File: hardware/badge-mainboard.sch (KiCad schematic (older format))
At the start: 11 parts

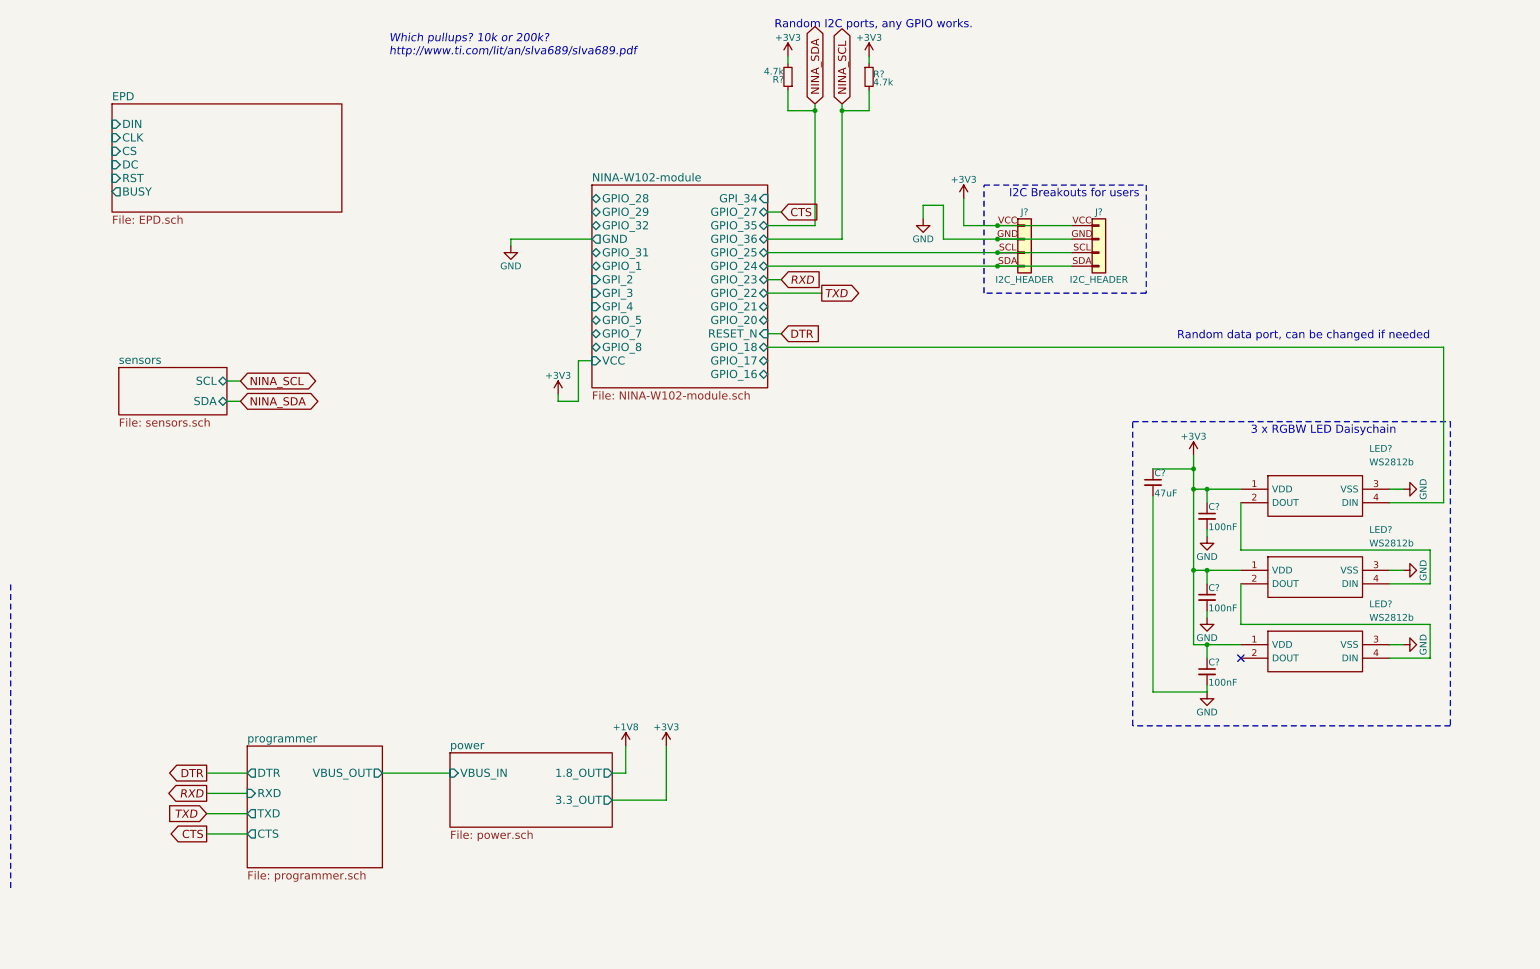
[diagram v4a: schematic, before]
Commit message: Added 4 user buttons
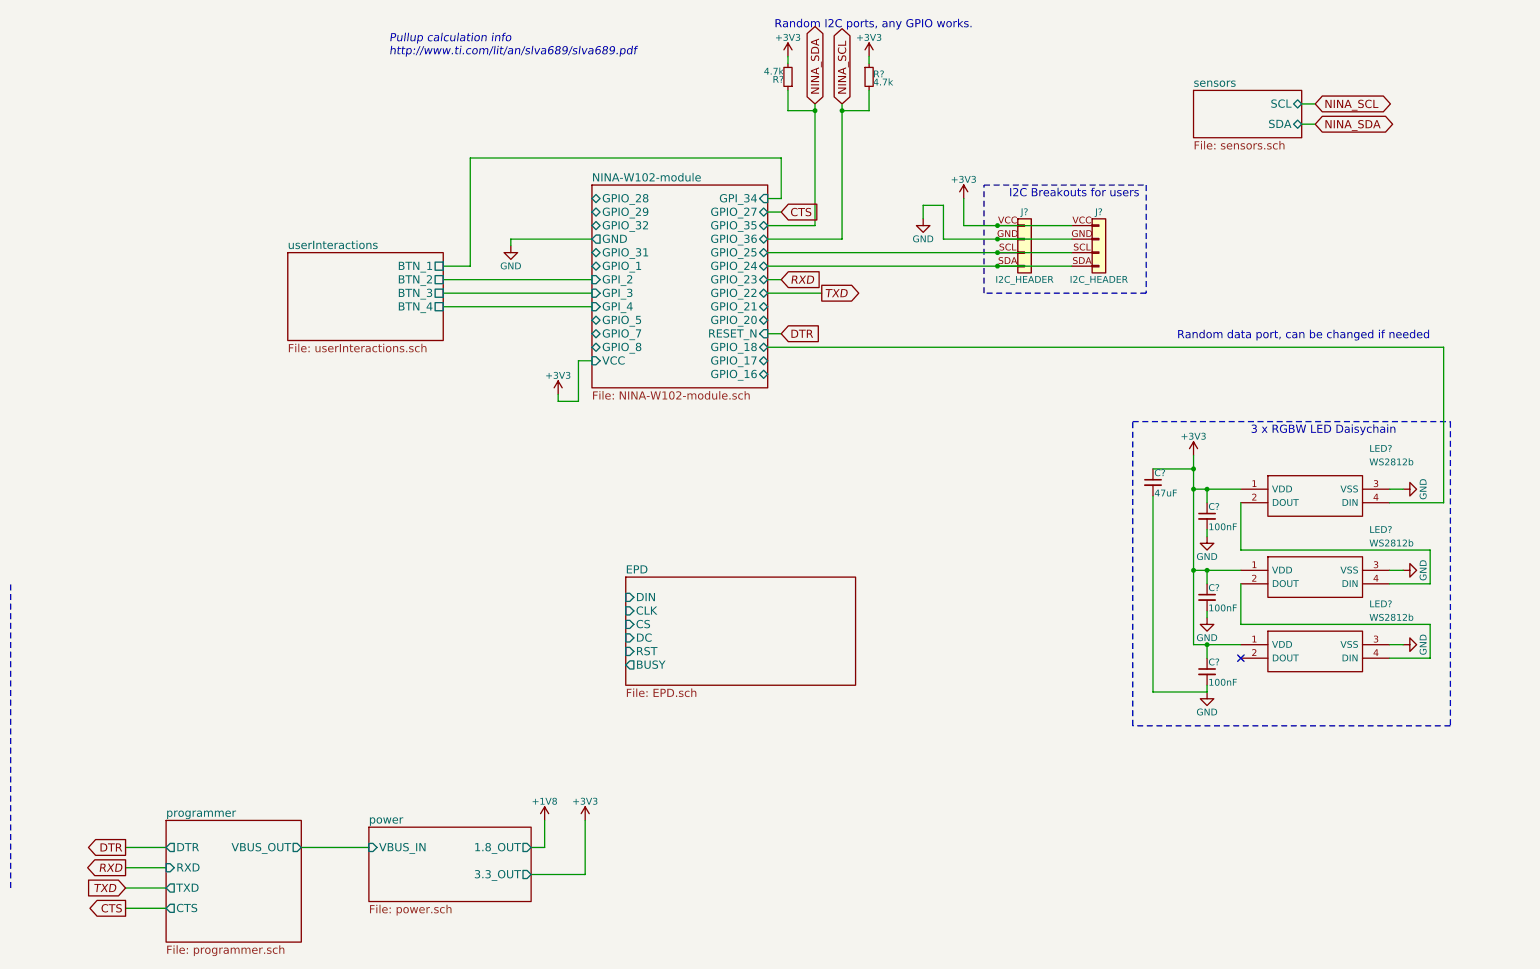
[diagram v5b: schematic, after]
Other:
- note added: "Pullup calculation info\nhttp://www.ti.com/lit/an/slva689/slva689.pdf"
- note removed: "Which pullups? 10k or 200k?\nhttp://www.ti.com/lit/an/slva689/slva689.pdf"
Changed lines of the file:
@@
 $Descr A4 11693 8268
 encoding utf-8
-Sheet 1 6
+Sheet 1 7
 Title "IoT conference badge - mainboard"
 Date "2018-04-09"
@@
 $EndComp
 Text Notes 3300 800  0    60   Italic 0
-Which pullups? 10k or 200k?\nhttp://www.ti.com/lit/an/slva689/slva689.pdf
+Pullup calculation info\nhttp://www.ti.com/lit/an/slva689/slva689.pdf
 $Sheet
-S 1300 3100 800  350
+S 9250 1050 800  350
 U 5AD378C9
 F0 "sensors" 60
 F1 "sensors.sch" 60
-F2 "SCL" B R 2100 3200 60
-F3 "SDA" B R 2100 3350 60
+F2 "SCL" B R 10050 1150 60
+F3 "SDA" B R 10050 1300 60
 $EndSheet
-Text GLabel 2200 3350 2    60   BiDi ~ 0
+Text GLabel 10150 1300 2    60   BiDi ~ 0
 NINA_SDA
-Text GLabel 2200 3200 2    60   BiDi ~ 0
+Text GLabel 10150 1150 2    60   BiDi ~ 0
 NINA_SCL
 $Sheet
-S 2250 5900 1000 900
+S 1650 6450 1000 900
 U 5AD3BA03
 F0 "programmer" 60
 F1 "programmer.sch" 60
-F2 "DTR" O L 2250 6100 60
-F3 "RXD" I L 2250 6250 60
-F4 "TXD" O L 2250 6400 60
-F5 "CTS" O L 2250 6550 60
-F6 "VBUS_OUT" O R 3250 6100 60
+F2 "DTR" O L 1650 6650 60
+F3 "RXD" I L 1650 6800 60
+F4 "TXD" O L 1650 6950 60
+F5 "CTS" O L 1650 7100 60
+F6 "VBUS_OUT" O R 2650 6650 60
 $EndSheet
-Text GLabel 1950 6400 0    60   Input Italic 0
+Text GLabel 1350 6950 0    60   Input Italic 0
 TXD
-Text GLabel 1950 6250 0    60   Output Italic 0
+Text GLabel 1350 6800 0    60   Output Italic 0
 RXD
 $Sheet
-S 1250 1150 1700 800
+S 5050 4650 1700 800
 U 5AD3E430
 F0 "EPD" 60
 F1 "EPD.sch" 60
-F2 "DIN" I L 1250 1300 60
-F3 "CLK" I L 1250 1400 60
-F4 "CS" I L 1250 1500 60
-F5 "DC" I L 1250 1600 60
-F6 "RST" I L 1250 1700 60
-F7 "BUSY" O L 1250 1800 60
+F2 "DIN" I L 5050 4800 60
+F3 "CLK" I L 5050 4900 60
+F4 "CS" I L 5050 5000 60
+F5 "DC" I L 5050 5100 60
+F6 "RST" I L 5050 5200 60
+F7 "BUSY" O L 5050 5300 60
 $EndSheet
 $Sheet
-S 3750 5950 1200 550
+S 3150 6500 1200 550
 U 5AD42326
 F0 "power" 60
 F1 "power.sch" 60
-F2 "VBUS_IN" I L 3750 6100 60
-F3 "1.8_OUT" O R 4950 6100 60
-F4 "3.3_OUT" O R 4950 6300 60
+F2 "VBUS_IN" I L 3150 6650 60
+F3 "1.8_OUT" O R 4350 6650 60
+F4 "3.3_OUT" O R 4350 6850 60
 $EndSheet
 $Comp
 L +1V8 #PWR08
 U 1 1 5AD43521
-P 5050 5900
-F 0 "#PWR08" H 5050 5750 50  0001 C CNN
-F 1 "+1V8" H 5050 6040 50  0000 C CNN
-F 2 "" H 5050 5900 50  0001 C CNN
-F 3 "" H 5050 5900 50  0001 C CNN
-	1    5050 5900
+P 4450 6450
+F 0 "#PWR08" H 4450 6300 50  0001 C CNN
+F 1 "+1V8" H 4450 6590 50  0000 C CNN
+F 2 "" H 4450 6450 50  0001 C CNN
+F 3 "" H 4450 6450 50  0001 C CNN
+	1    4450 6450
 	1    0    0    -1
 $EndComp
@@
 L +3V3 #PWR09
 U 1 1 5AD44887
-P 5350 5900
-F 0 "#PWR09" H 5350 5750 50  0001 C CNN
-F 1 "+3V3" H 5350 6040 50  0000 C CNN
-F 2 "" H 5350 5900 50  0001 C CNN
-F 3 "" H 5350 5900 50  0001 C CNN
-	1    5350 5900
+P 4750 6450
+F 0 "#PWR09" H 4750 6300 50  0001 C CNN
+F 1 "+3V3" H 4750 6590 50  0000 C CNN
+F 2 "" H 4750 6450 50  0001 C CNN
+F 3 "" H 4750 6450 50  0001 C CNN
+	1    4750 6450
 	1    0    0    -1
 $EndComp
@@
 Text Notes 8850 1850 2    60   ~ 0
 I2C Breakouts for users
-Text GLabel 1950 6550 0    60   Output ~ 0
+Text GLabel 1350 7100 0    60   Output ~ 0
 CTS
-Text GLabel 1950 6100 0    60   Output ~ 0
+Text GLabel 1350 6650 0    60   Output ~ 0
 DTR
 Wire Notes Line
@@
 Connection ~ 6450 1200
 Wire Wire Line
-	2100 3200 2200 3200
-Wire Wire Line
-	2100 3350 2200 3350
-Wire Wire Line
-	1950 6250 2250 6250
-Wire Wire Line
-	1950 6400 2250 6400
-Wire Wire Line
-	3250 6100 3750 6100
-Wire Wire Line
-	4950 6100 5050 6100
-Wire Wire Line
-	5050 6100 5050 5900
-Wire Wire Line
-	4950 6300 5350 6300
-Wire Wire Line
-	5350 6300 5350 5900
+	10050 1150 10150 1150
+Wire Wire Line
+	10050 1300 10150 1300
+Wire Wire Line
+	1350 6800 1650 6800
+Wire Wire Line
+	1350 6950 1650 6950
+Wire Wire Line
+	2650 6650 3150 6650
+Wire Wire Line
+	4350 6650 4450 6650
+Wire Wire Line
+	4450 6650 4450 6450
+Wire Wire Line
+	4350 6850 4750 6850
+Wire Wire Line
+	4750 6850 4750 6450
 Wire Wire Line
 	6450 1200 6250 1200
@@
 	8900 2550 7700 2550
 Wire Wire Line
-	1950 6100 2250 6100
-Wire Wire Line
-	2250 6550 1950 6550
+	1350 6650 1650 6650
+Wire Wire Line
+	1650 7100 1350 7100
 Text GLabel 6500 2550 2    60   Output Italic 0
 TXD
@@
 Wire Wire Line
 	6500 2550 6100 2550
+$Sheet
+S 2550 2250 1150 650
+U 5AE85D2E
+F0 "userInteractions" 60
+F1 "userInteractions.sch" 60
+F2 "BTN_1" U R 3700 2350 60
+F3 "BTN_2" U R 3700 2450 60
+F4 "BTN_3" U R 3700 2550 60
+F5 "BTN_4" U R 3700 2650 60
+$EndSheet
+Wire Wire Line
+	4800 2450 3700 2450
+Wire Wire Line
+	4800 2550 3700 2550
+Wire Wire Line
+	4800 2650 3700 2650
+Wire Wire Line
+	3700 2350 3900 2350
+Wire Wire Line
+	3900 2350 3900 1550
+Wire Wire Line
+	3900 1550 6200 1550
+Wire Wire Line
+	6200 1550 6200 1850
+Wire Wire Line
+	6200 1850 6100 1850
 $EndSCHEMATC

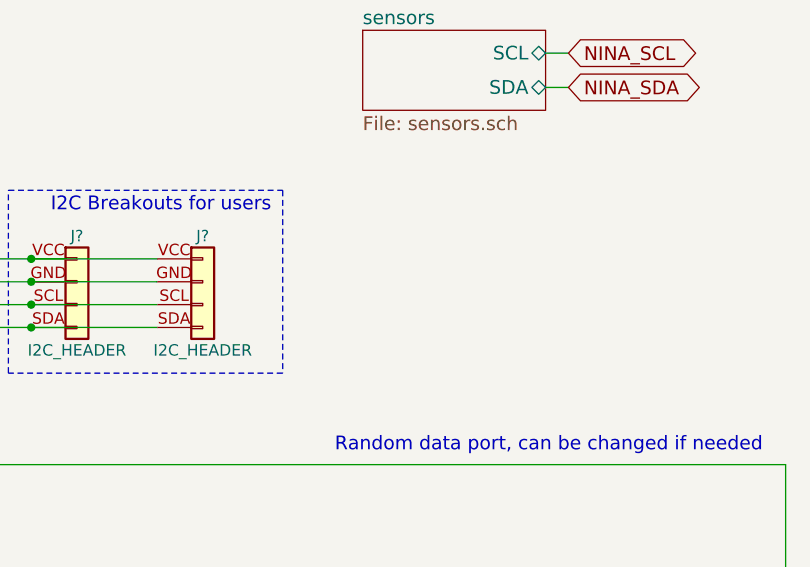
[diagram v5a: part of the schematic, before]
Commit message: added missing sub schema file and comments
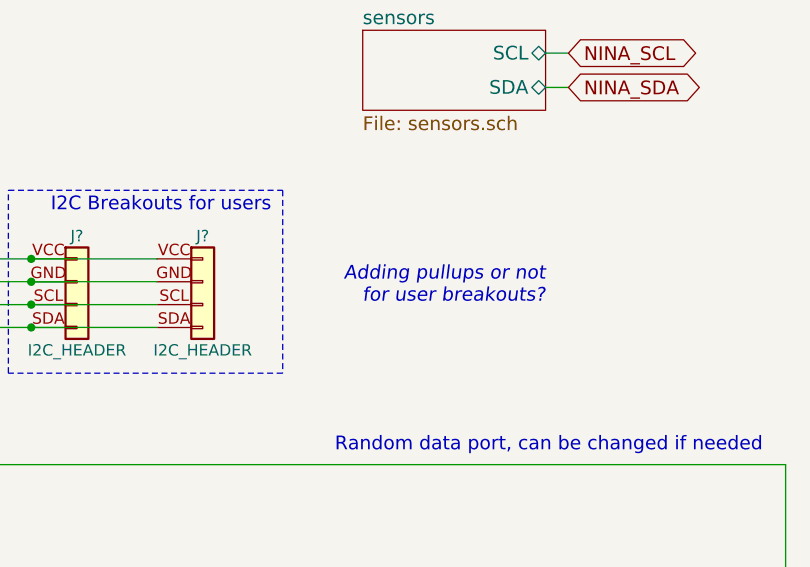
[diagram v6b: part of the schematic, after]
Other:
- note added: "Adding pullups or not\nfor user breakouts?"
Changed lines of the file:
@@
 Wire Wire Line
 	6200 1850 6100 1850
+Text Notes 10050 2250 2    60   Italic 0
+Adding pullups or not\nfor user breakouts?
 $EndSCHEMATC

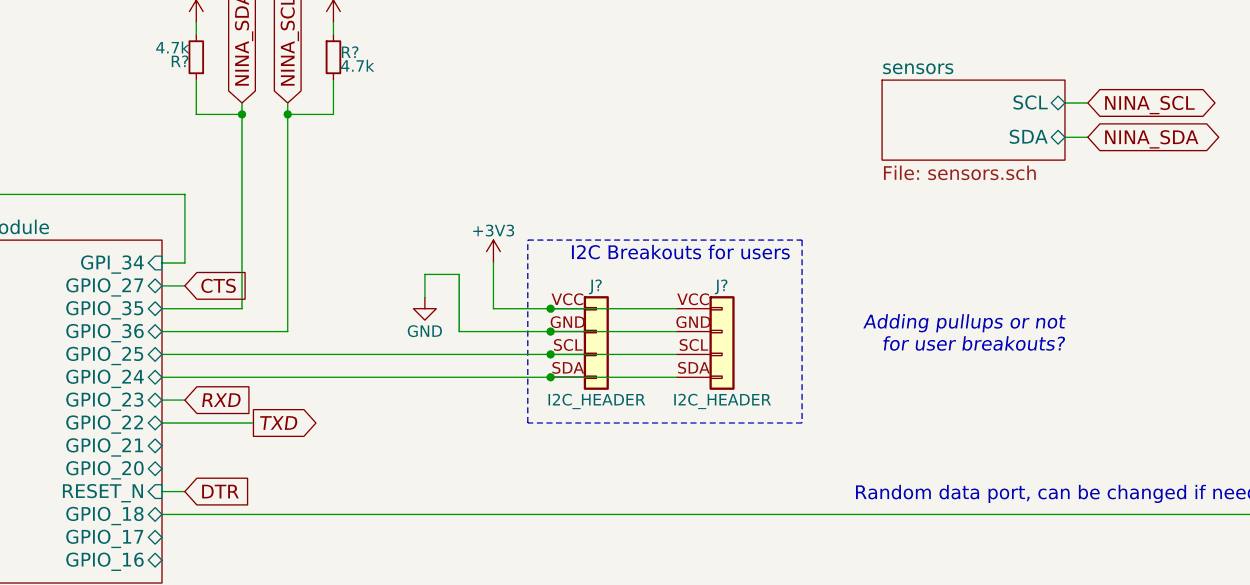
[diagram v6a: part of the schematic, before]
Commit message: Added unpopulated user pullups for I2C user bus
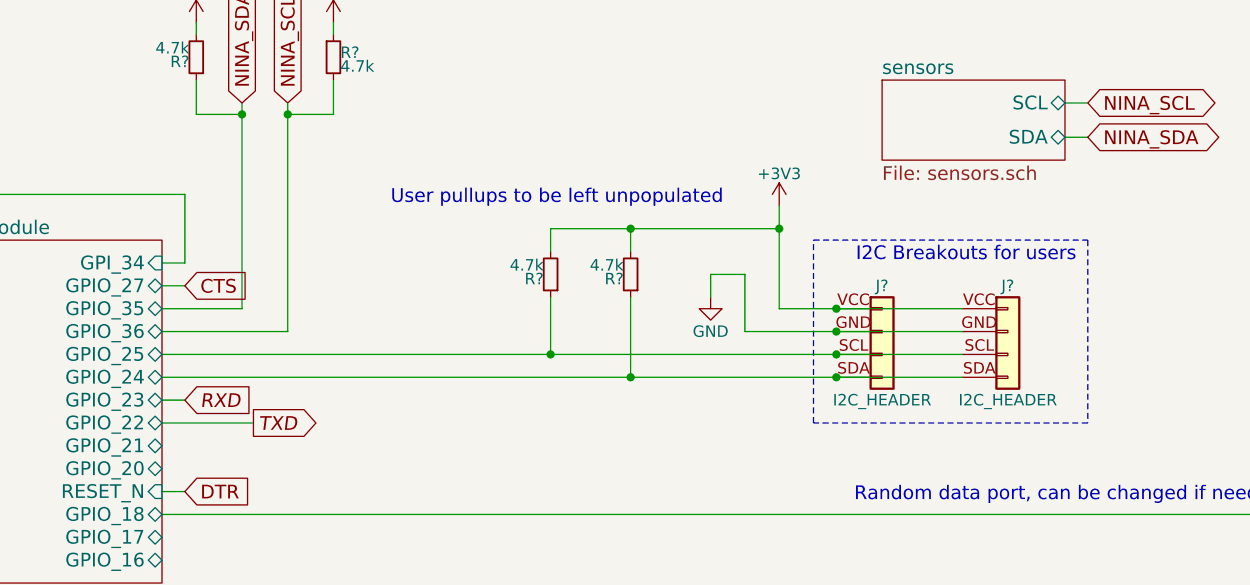
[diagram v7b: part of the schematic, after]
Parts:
- added R? (x2): 4.7k, symbol R_Small
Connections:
- net +3V3: now also R?.2, R?.2
- net NINA-W102-module/GPIO_24: now also R?.1
- net NINA-W102-module/GPIO_25: now also R?.1
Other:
- note added: "User pullups to be left unpopulated"
- note removed: "Adding pullups or not\nfor user breakouts?"
- moved on the sheet: J?
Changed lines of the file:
@@
 L I2C_HEADER J?
 U 1 1 5AE74CFE
-P 8000 2150
-F 0 "J?" H 8000 2350 50  0000 C CNN
-F 1 "I2C_HEADER" H 8000 1850 50  0000 C CNN
-F 2 "" H 8000 2150 50  0001 C CNN
-F 3 "" H 8000 2150 50  0001 C CNN
-	1    8000 2150
+P 9250 2150
+F 0 "J?" H 9250 2350 50  0000 C CNN
+F 1 "I2C_HEADER" H 9250 1850 50  0000 C CNN
+F 2 "" H 9250 2150 50  0001 C CNN
+F 3 "" H 9250 2150 50  0001 C CNN
+	1    9250 2150
 	1    0    0    -1
 $EndComp
@@
 L I2C_HEADER J?
 U 1 1 5AE74E55
-P 8550 2150
-F 0 "J?" H 8550 2350 50  0000 C CNN
-F 1 "I2C_HEADER" H 8550 1850 50  0000 C CNN
-F 2 "" H 8550 2150 50  0001 C CNN
-F 3 "" H 8550 2150 50  0001 C CNN
-	1    8550 2150
+P 9800 2150
+F 0 "J?" H 9800 2350 50  0000 C CNN
+F 1 "I2C_HEADER" H 9800 1850 50  0000 C CNN
+F 2 "" H 9800 2150 50  0001 C CNN
+F 3 "" H 9800 2150 50  0001 C CNN
+	1    9800 2150
 	1    0    0    -1
 $EndComp
@@
 L +3V3 #PWR?
 U 1 1 5AE75A47
-P 7550 1850
-F 0 "#PWR?" H 7550 1700 50  0001 C CNN
-F 1 "+3V3" H 7550 1990 50  0000 C CNN
-F 2 "" H 7550 1850 50  0001 C CNN
-F 3 "" H 7550 1850 50  0001 C CNN
-	1    7550 1850
+P 8800 1600
+F 0 "#PWR?" H 8800 1450 50  0001 C CNN
+F 1 "+3V3" H 8800 1740 50  0000 C CNN
+F 2 "" H 8800 1600 50  0001 C CNN
+F 3 "" H 8800 1600 50  0001 C CNN
+	1    8800 1600
 	1    0    0    -1
 $EndComp
@@
 L GND #PWR?
 U 1 1 5AE75B75
-P 7250 2000
-F 0 "#PWR?" H 7250 1750 50  0001 C CNN
-F 1 "GND" H 7250 1850 50  0000 C CNN
-F 2 "" H 7250 2000 50  0001 C CNN
-F 3 "" H 7250 2000 50  0001 C CNN
-	1    7250 2000
-	1    0    0    -1
-$EndComp
-Text Notes 8850 1850 2    60   ~ 0
+P 8500 2000
+F 0 "#PWR?" H 8500 1750 50  0001 C CNN
+F 1 "GND" H 8500 1850 50  0000 C CNN
+F 2 "" H 8500 2000 50  0001 C CNN
+F 3 "" H 8500 2000 50  0001 C CNN
+	1    8500 2000
+	1    0    0    -1
+$EndComp
+Text Notes 10100 1850 2    60   ~ 0
 I2C Breakouts for users
 Text GLabel 1350 7100 0    60   Output ~ 0
@@
 	4200 2150 4200 2200
 Wire Wire Line
-	6100 2250 8350 2250
-Wire Wire Line
-	6100 2350 8350 2350
-Connection ~ 7800 2350
-Connection ~ 7800 2250
-Wire Wire Line
-	7550 2050 8350 2050
-Wire Wire Line
-	7550 2050 7550 1850
-Wire Wire Line
-	7400 2150 8350 2150
-Wire Wire Line
-	7400 2150 7400 1900
-Wire Wire Line
-	7400 1900 7250 1900
-Wire Wire Line
-	7250 1900 7250 2000
-Connection ~ 7800 2150
-Connection ~ 7800 2050
-Wire Notes Line
-	7700 2550 7700 1750
-Wire Notes Line
-	7700 1750 8900 1750
-Wire Notes Line
-	8900 1750 8900 2550
-Wire Notes Line
-	8900 2550 7700 2550
+	6100 2250 9600 2250
+Wire Wire Line
+	6100 2350 9600 2350
+Connection ~ 9050 2350
+Connection ~ 9050 2250
+Wire Wire Line
+	8800 2050 9600 2050
+Wire Wire Line
+	8800 1600 8800 2050
+Wire Wire Line
+	8650 2150 9600 2150
+Wire Wire Line
+	8650 2150 8650 1900
+Wire Wire Line
+	8650 1900 8500 1900
+Wire Wire Line
+	8500 1900 8500 2000
+Connection ~ 9050 2150
+Connection ~ 9050 2050
+Wire Notes Line
+	8950 2550 8950 1750
+Wire Notes Line
+	8950 1750 10150 1750
+Wire Notes Line
+	10150 1750 10150 2550
+Wire Notes Line
+	10150 2550 8950 2550
 Wire Wire Line
 	1350 6650 1650 6650
@@
 Wire Wire Line
 	6200 1850 6100 1850
-Text Notes 10050 2250 2    60   Italic 0
-Adding pullups or not\nfor user breakouts?
+$Comp
+L R_Small R?
+U 1 1 5AE91D89
+P 7800 1900
+F 0 "R?" H 7830 1920 50  0000 L CNN
+F 1 "4.7k" H 7830 1860 50  0000 L CNN
+F 2 "" H 7800 1900 50  0001 C CNN
+F 3 "" H 7800 1900 50  0001 C CNN
+	1    7800 1900
+	-1   0    0    1
+$EndComp
+$Comp
+L R_Small R?
+U 1 1 5AE91F41
+P 8150 1900
+F 0 "R?" H 8180 1920 50  0000 L CNN
+F 1 "4.7k" H 8180 1860 50  0000 L CNN
+F 2 "" H 8150 1900 50  0001 C CNN
+F 3 "" H 8150 1900 50  0001 C CNN
+	1    8150 1900
+	-1   0    0    1
+$EndComp
+Wire Wire Line
+	7800 2000 7800 2250
+Connection ~ 7800 2250
+Wire Wire Line
+	8150 2000 8150 2350
+Connection ~ 8150 2350
+Wire Wire Line
+	8150 1800 8150 1700
+Wire Wire Line
+	7800 1700 8800 1700
+Connection ~ 8800 1700
+Wire Wire Line
+	7800 1800 7800 1700
+Connection ~ 8150 1700
+Text Notes 7100 1600 0    60   ~ 0
+User pullups to be left unpopulated
 $EndSCHEMATC
